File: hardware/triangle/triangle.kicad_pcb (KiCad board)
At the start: 4 copper layers, 100 x 86.6 mm, 71 parts, among them J1 USB_C_Receptacle_USB2.0_16P, J2 USB_C_Receptacle_USB2.0_16P, U2 EA8212HT6R

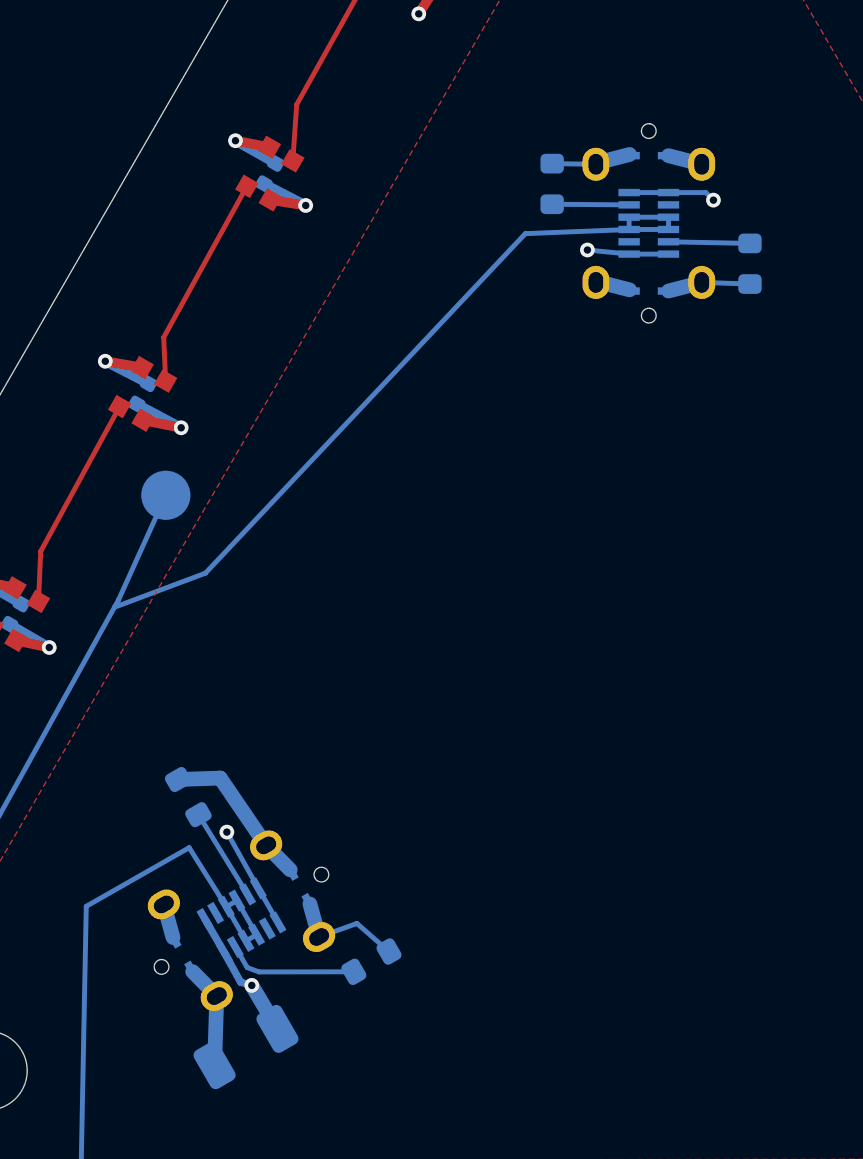
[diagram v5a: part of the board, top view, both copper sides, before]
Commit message: add another capacitor
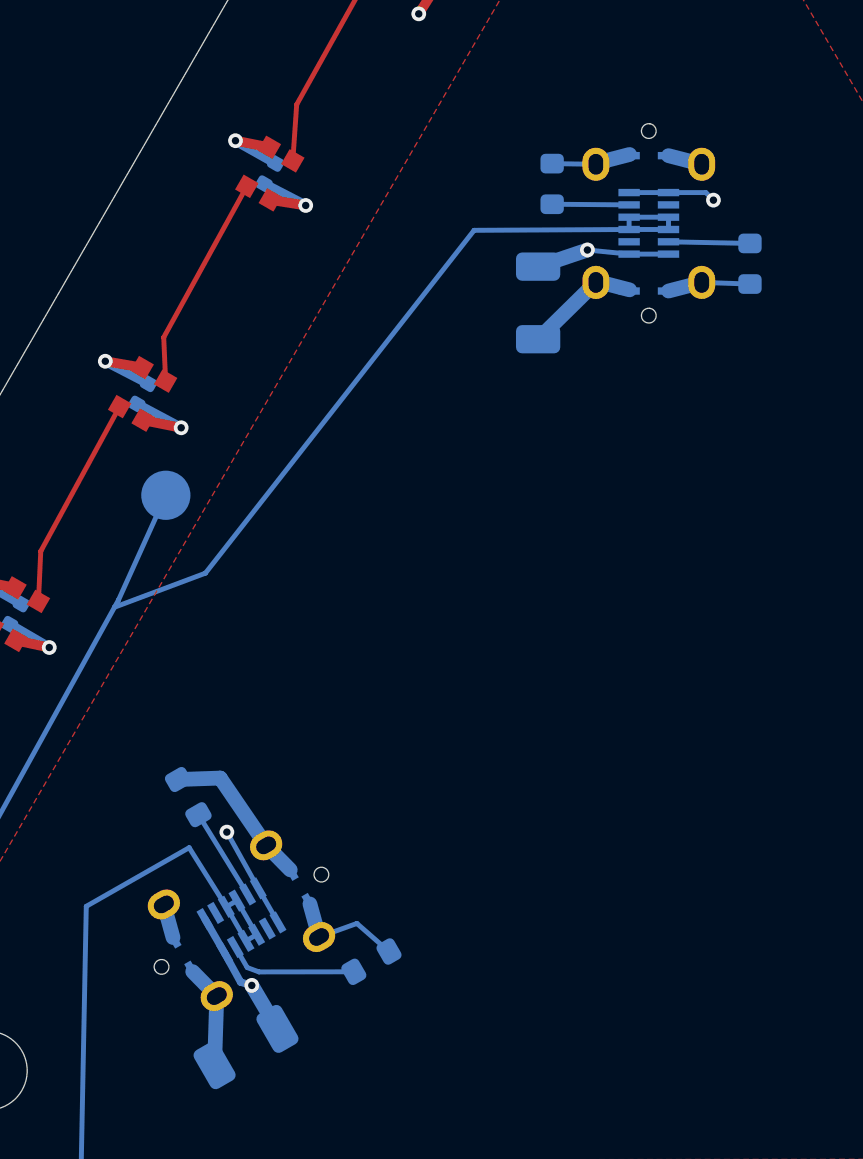
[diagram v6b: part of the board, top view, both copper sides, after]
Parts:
- added C29: 47µF, Capacitor_SMD:C_1206_3216Metric, B.Cu at (145.4, 105.5)
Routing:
- net GND: track 104.7 -> 108.0 mm
- net +12V: track 26.3 -> 28.5 mm
- net LED_DATA_OUT: track 63.9 -> 64.7 mm
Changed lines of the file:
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@@
 		)
 		(pad "0" thru_hole oval
-			(at -2.4 -2.15 120)
+			(at -2.4 -2.15 300)
 			(size 1.1 1.35)
 			(drill oval 0.6 0.85)
@@
 		)
 		(pad "0" thru_hole oval
-			(at -2.4 2.15 120)
+			(at -2.4 2.15 300)
 			(size 1.1 1.35)
 			(drill oval 0.6 0.85)
@@
 		)
 		(pad "0" thru_hole oval
-			(at 2.4 -2.15 120)
+			(at 2.4 -2.15 300)
 			(size 1.1 1.35)
 			(drill oval 0.6 0.85)
@@
 		)
 		(pad "0" thru_hole oval
-			(at 2.4 2.15 120)
+			(at 2.4 2.15 300)
 			(size 1.1 1.35)
 			(drill oval 0.6 0.85)
@@
 		)
 	)
+	(footprint "Capacitor_SMD:C_1206_3216Metric"
+		(layer "B.Cu")
+		(at 145.399531 105.503314 90)
+		(descr "Capacitor SMD 1206 (3216 Metric), square (rectangular) end terminal, IPC-7351 nominal, (Body size source: IPC-SM-782 page 76, https://www.pcb-3d.com/wordpress/wp-content/uploads/ipc-sm-782a_amendment_1_and_2.pdf)")
+		(tags "capacitor")
+		(property "Reference" "C29"
+			(at -0.609211 -1.971616 90)
+			(layer "B.SilkS")
+			(effects
+				(font
+					(size 1 1)
+					(thickness 0.15)
+				)
+				(justify mirror)
+			)
+		)
+		(property "Value" "47µF"
+			(at 0 -1.85 90)
+			(layer "B.Fab")
+			(effects
+				(font
+					(size 1 1)
+					(thickness 0.15)
+				)
+				(justify mirror)
+			)
+		)
+		(property "Datasheet" ""
+			(at 0 0 90)
+			(layer "B.Fab")
+			(hide yes)
+			(effects
+				(font
+					(size 1.27 1.27)
+				)
+				(justify mirror)
+			)
+		)
+		(property "Description" ""
+			(at 0 0 90)
+			(layer "B.Fab")
+			(hide yes)
+			(effects
+				(font
+					(size 1.27 1.27)
+				)
+				(justify mirror)
+			)
+		)
+		(property "KiLib_Generator" "SMD_2terminal_chip_molded"
+			(at 0 0 90)
+			(layer "B.SilkS")
+			(hide yes)
+			(effects
+				(font
+					(size 1 1)
+					(thickness 0.15)
+				)
+				(justify mirror)
+			)
+		)
+		(property ki_fp_filters "C_*")
+		(sheetname "/")
+		(sheetfile "usb_and_power.kicad_sch")
+		(units
+			(unit
+				(name "A")
+				(pins "1" "2")
+			)
+		)
+		(attr smd)
+		(duplicate_pad_numbers_are_jumpers no)
+		(fp_line
+			(start -0.711252 -0.91)
+			(end 0.711252 -0.91)
+			(stroke
+				(width 0.12)
+				(type solid)
+			)
+			(layer "B.SilkS")
+		)
+		(fp_line
+			(start -0.711252 0.91)
+			(end 0.711252 0.91)
+			(stroke
+				(width 0.12)
+				(type solid)
+			)
+			(layer "B.SilkS")
+		)
+		(fp_rect
+			(start -2.3 1.15)
+			(end 2.3 -1.15)
+			(stroke
+				(width 0.05)
+				(type solid)
+			)
+			(fill no)
+			(layer "B.CrtYd")
+		)
+		(fp_rect
+			(start -1.6 0.8)
+			(end 1.6 -0.8)
+			(stroke
+				(width 0.1)
+				(type solid)
+			)
+			(fill no)
+			(layer "B.Fab")
+		)
+		(fp_text user "${REFERENCE}"
+			(at 0 0 90)
+			(layer "B.Fab")
+			(effects
+				(font
+					(size 0.8 0.8)
+					(thickness 0.12)
+				)
+				(justify mirror)
+			)
+		)
+		(pad "1" smd roundrect
+			(at -1.475 0 90)
+			(size 1.15 1.8)
+			(layers "B.Cu" "B.Mask" "B.Paste")
+			(roundrect_rratio 0.217391)
+			(net "GND")
+			(pintype "passive")
+		)
+		(pad "2" smd roundrect
+			(at 1.475 0 90)
+			(size 1.15 1.8)
+			(layers "B.Cu" "B.Mask" "B.Paste")
+			(roundrect_rratio 0.217391)
+			(net "+12V")
+			(pintype "passive")
+		)
+		(embedded_fonts no)
+		(model "${KICAD10_3DMODEL_DIR}/Capacitor_SMD.3dshapes/C_1206_3216Metric.step"
+			(offset
+				(xyz 0 0 0)
+			)
+			(scale
+				(xyz 1 1 1)
+			)
+			(rotate
+				(xyz 0 0 0)
+			)
+		)
+	)
 	(footprint "footprints:TYPE-C-SMD_USB4120-03-C"
 		(layer "B.Cu")
@@
 		)
 		(pad "0" thru_hole oval
-			(at -2.4 -2.15)
+			(at -2.4 -2.15 180)
 			(size 1.1 1.35)
 			(drill oval 0.6 0.85)
@@
 		)
 		(pad "0" thru_hole oval
-			(at -2.4 2.15)
+			(at -2.4 2.15 180)
 			(size 1.1 1.35)
 			(drill oval 0.6 0.85)
@@
 		)
 		(pad "0" thru_hole oval
-			(at 2.4 -2.15)
+			(at 2.4 -2.15 180)
 			(size 1.1 1.35)
 			(drill oval 0.6 0.85)
@@
 		)
 		(pad "0" thru_hole oval
-			(at 2.4 2.15)
+			(at 2.4 2.15 180)
 			(size 1.1 1.35)
 			(drill oval 0.6 0.85)
@@
 	)
 	(segment
+		(start 147.746593 104.669695)
+		(end 145.399531 106.978314)
+		(width 0.6)
+		(layer "B.Cu")
+		(net "GND")
+	)
+	(segment
 		(start 150.487662 143.115658)
 		(end 150.487662 144.992338)
@@
 	)
 	(segment
-		(start 144.879443 102.688609)
-		(end 131.88101 116.484287)
-		(width 0.2)
-		(layer "B.Cu")
-		(net "LED_DATA_OUT")
-	)
-	(segment
-		(start 149.096593 102.519695)
-		(end 144.879443 102.688609)
+		(start 150.696593 102.019695)
+		(end 150.696593 102.519695)
 		(width 0.2)
 		(layer "B.Cu")
@@
 	)
 	(segment
-		(start 150.696593 102.019695)
-		(end 150.696593 102.519695)
+		(start 131.88101 116.484287)
+		(end 128.186554 117.868259)
 		(width 0.2)
 		(layer "B.Cu")
@@
 	)
 	(segment
-		(start 131.88101 116.484287)
-		(end 128.186554 117.868259)
+		(start 149.096593 102.519695)
+		(end 142.798111 102.553285)
 		(width 0.2)
 		(layer "B.Cu")
@@
 	)
 	(segment
+		(start 142.798111 102.553285)
+		(end 131.88101 116.484287)
+		(width 0.2)
+		(layer "B.Cu")
+		(net "LED_DATA_OUT")
+	)
+	(segment
 		(start 128.186554 117.868259)
 		(end 128.350952 117.570911)
@@
 		(net "+12V")
 	)
+	(segment
+		(start 145.399531 104.028314)
+		(end 147.402345 103.35256)
+		(width 0.6)
+		(layer "B.Cu")
+		(net "+12V")
+	)

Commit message: fix labels
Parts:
- TP1 4V: renamed from TP1-4V1
- TP2 DATA_IN: renamed from TP2-LED_DATA_IN1
- TP3 DATA_OUT: renamed from TP3-LED_DATA_OUT1
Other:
- board text added: "IN"
- board text added: "OUT"
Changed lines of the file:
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@@
 		(descr "SMD pad as test Point, diameter 2.0mm")
 		(tags "test point SMD pad")
-		(property "Reference" "TP1-4V1"
-			(at 0 1.998 180)
+		(property "Reference" "TP1 4V"
+			(at -0.031838 2.307368 180)
 			(layer "B.SilkS")
 			(effects
@@
 		(descr "SMD pad as test Point, diameter 2.0mm")
 		(tags "test point SMD pad")
-		(property "Reference" "TP2-LED_DATA_IN1"
-			(at 3.666008 -3.245258 180)
+		(property "Reference" "TP2 DATA_IN"
+			(at 0.310921 -3.172804 180)
 			(layer "B.SilkS")
 			(effects
@@
 		(descr "SMD pad as test Point, diameter 2.0mm")
 		(tags "test point SMD pad")
-		(property "Reference" "TP3-LED_DATA_OUT1"
-			(at 9.43352 -0.15821 180)
+		(property "Reference" "TP3 DATA_OUT"
+			(at 1.647798 2.701803 180)
 			(layer "B.SilkS")
 			(effects
@@
 		(layer "Edge.Cuts")
 	)
+	(gr_text "IN"
+		(at 143.721444 129.967482 0)
+		(layer "B.SilkS")
+		(effects
+			(font
+				(size 3 3)
+				(thickness 0.5)
+				(bold yes)
+			)
+			(justify left bottom mirror)
+		)
+	)
+	(gr_text "OUT"
+		(at 155.289075 111.574326 0)
+		(layer "B.SilkS")
+		(effects
+			(font
+				(size 3 3)
+				(thickness 0.5)
+				(bold yes)
+			)
+			(justify left bottom mirror)
+		)
+	)
 	(segment
